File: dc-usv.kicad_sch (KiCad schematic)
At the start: 0 parts

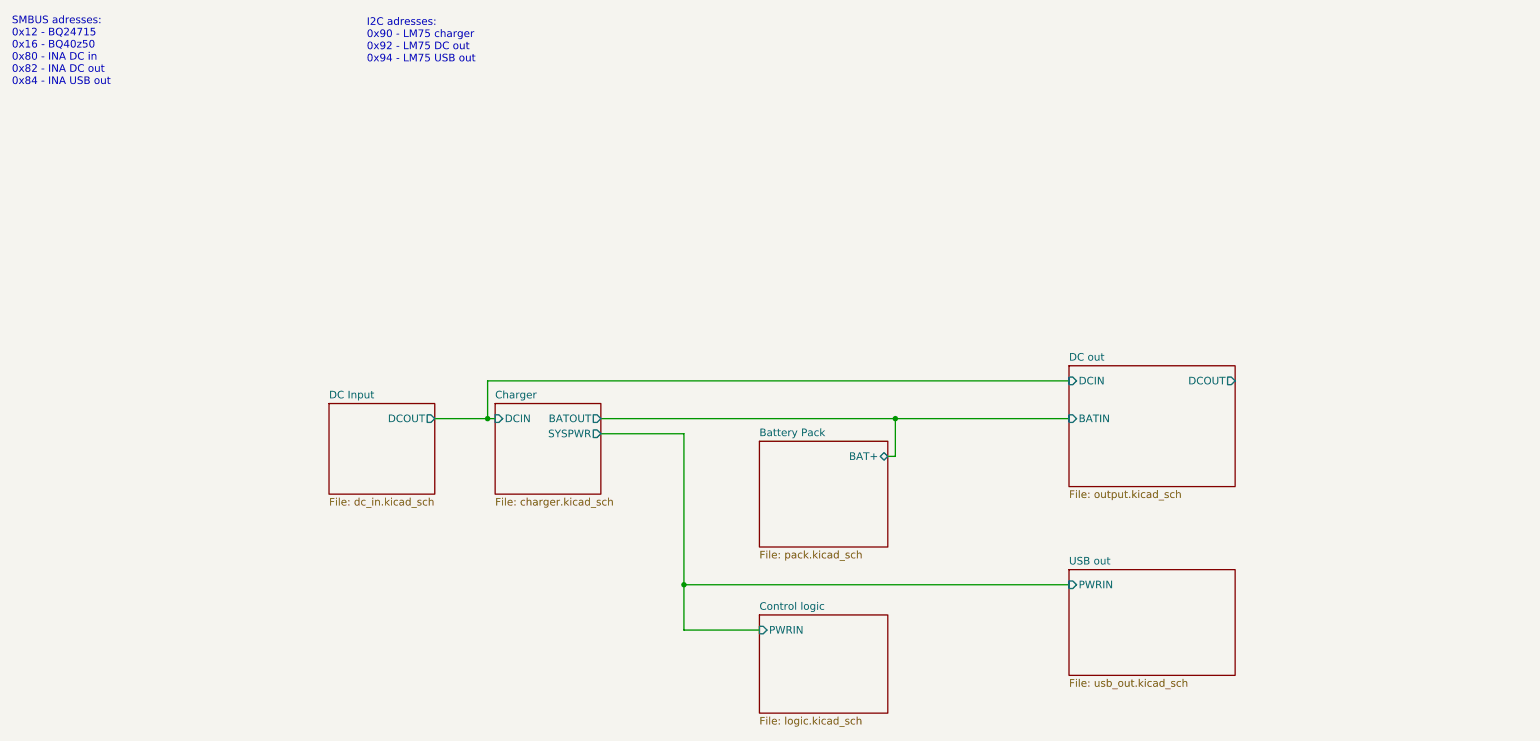
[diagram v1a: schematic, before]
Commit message: Finish DC output schematic capture
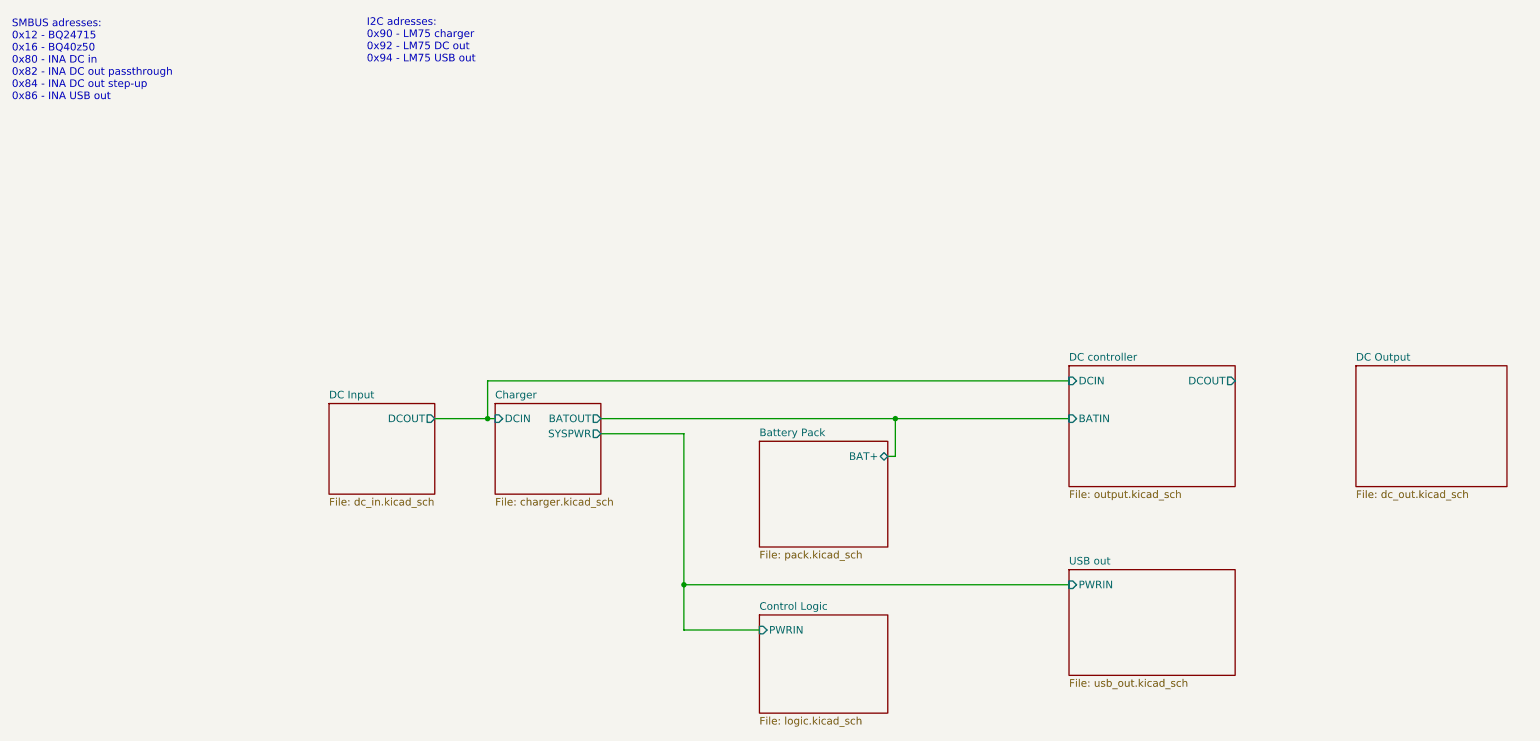
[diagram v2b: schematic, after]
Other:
- sheet Control logic renamed Control Logic
- sheet DC out renamed DC controller
- added sheet DC Output (dc_out.kicad_sch)
- note added: "SMBUS adresses: 0x12 - BQ24715 0x16 - BQ40z50 0x80 - INA DC in 0x82 - INA DC out passthrough 0x84 - INA DC out step-up 0x86 - INA USB out"
- note removed: "SMBUS adresses: 0x12 - BQ24715 0x16 - BQ40z50 0x80 - INA DC in 0x82 - INA DC out 0x84 - INA USB out"

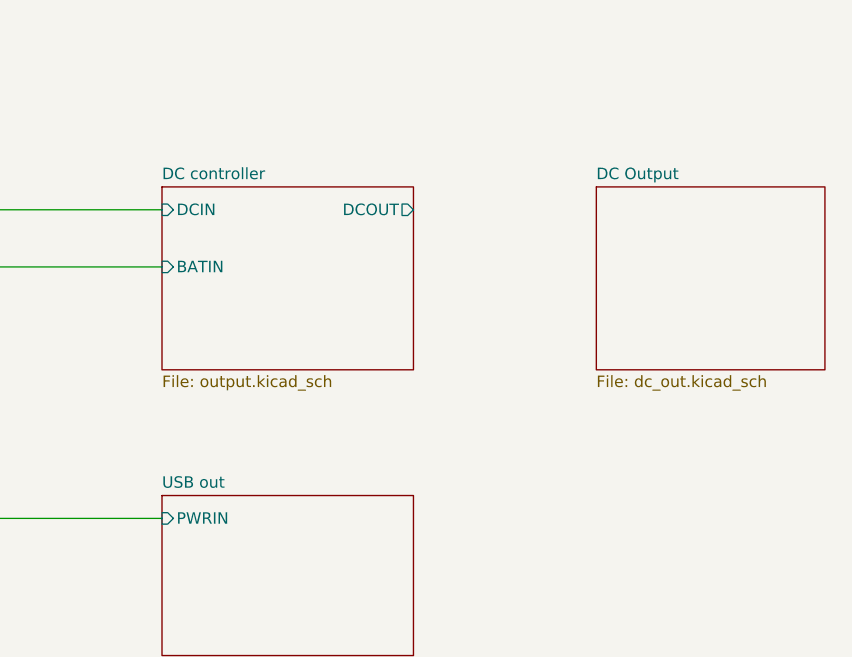
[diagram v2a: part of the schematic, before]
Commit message: Add barrel jack footprints
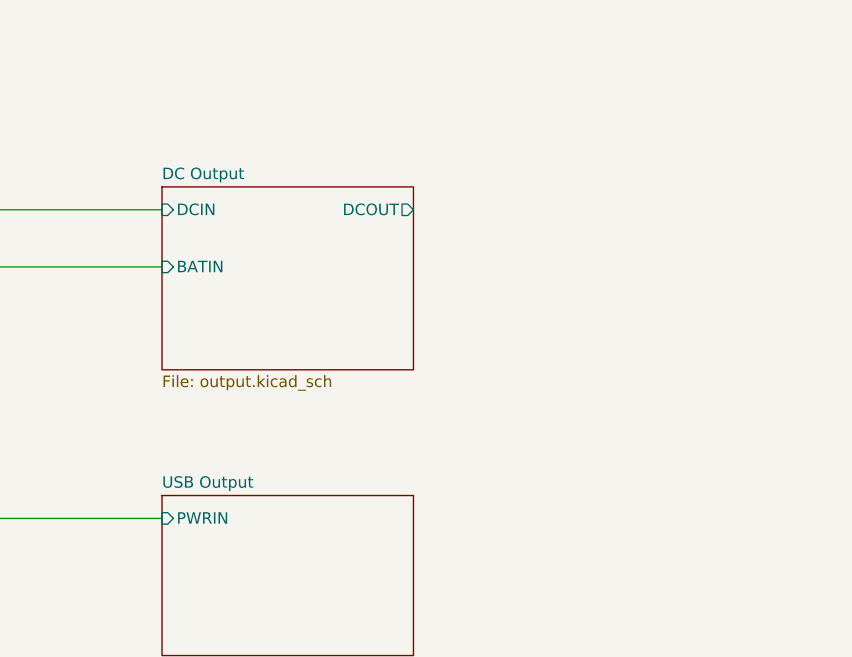
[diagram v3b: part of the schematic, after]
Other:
- sheet USB out renamed USB Output
- removed sheet DC controller
- sheet DC Output: file dc_out.kicad_sch -> output.kicad_sch
- sheet DC Output ports: added BATIN, DCIN, DCOUT; removed none

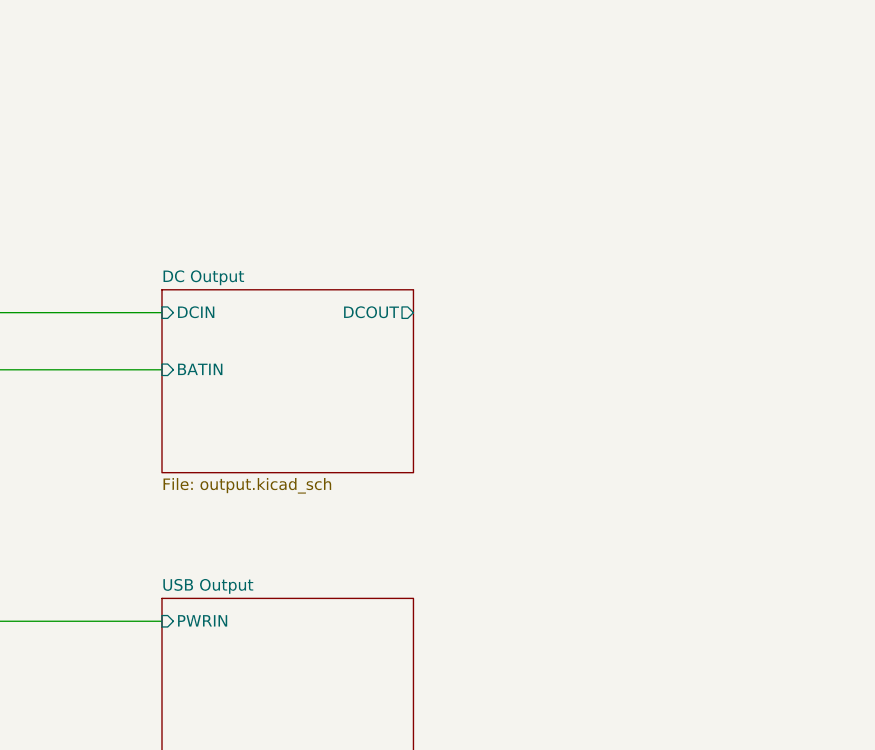
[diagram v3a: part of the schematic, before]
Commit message: Add individually switchable outputs
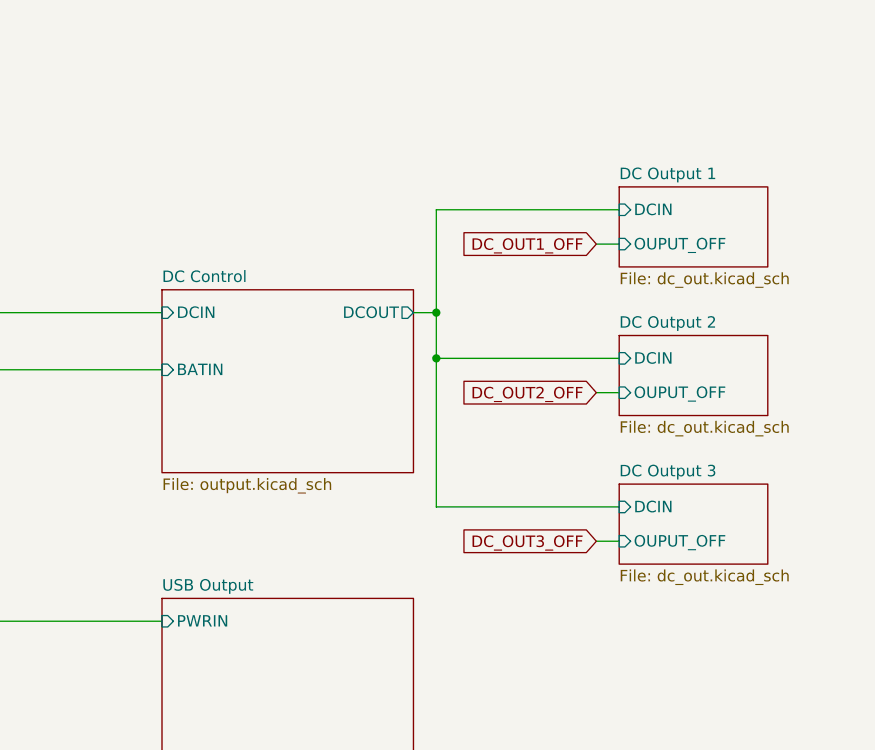
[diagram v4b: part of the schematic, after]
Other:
- sheet DC Output renamed DC Control
- added sheet DC Output 1 (dc_out.kicad_sch)
- added sheet DC Output 2 (dc_out.kicad_sch)
- added sheet DC Output 3 (dc_out.kicad_sch)

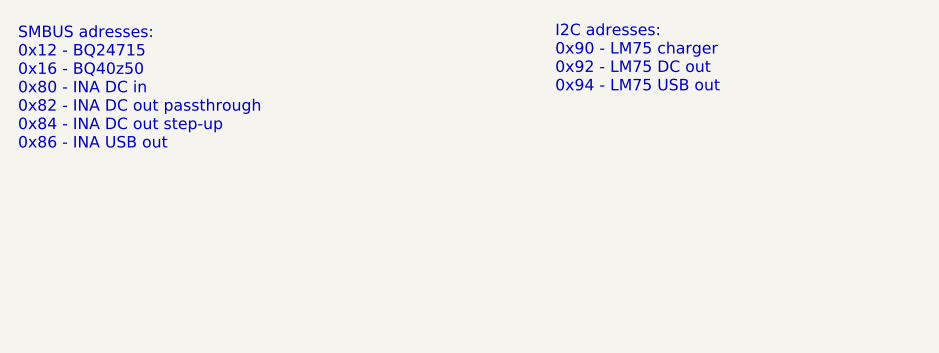
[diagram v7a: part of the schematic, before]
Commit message: Add 64x48 SSD1306 OLED
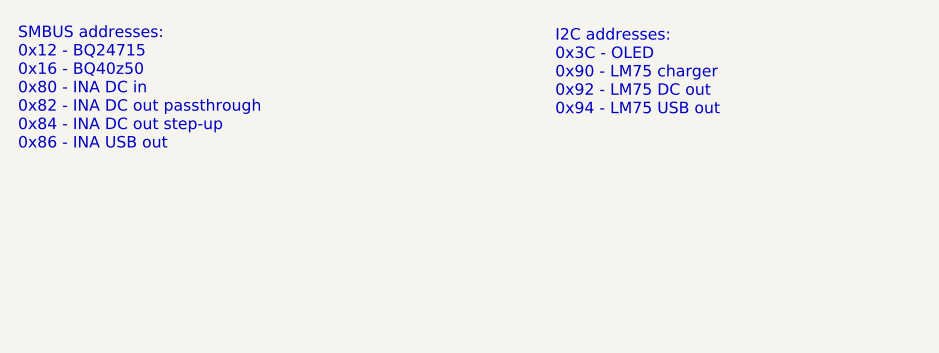
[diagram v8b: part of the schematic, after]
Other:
- note added: "I2C addresses: 0x3C - OLED 0x90 - LM75 charger 0x92 - LM75 DC out 0x94 - LM75 USB out"
- note added: "SMBUS addresses: 0x12 - BQ24715 0x16 - BQ40z50 0x80 - INA DC in 0x82 - INA DC out passthrough 0x84 - INA DC out step-up 0x86 - INA USB out"
- note removed: "I2C adresses: 0x90 - LM75 charger 0x92 - LM75 DC out 0x94 - LM75 USB out"
- note removed: "SMBUS adresses: 0x12 - BQ24715 0x16 - BQ40z50 0x80 - INA DC in 0x82 - INA DC out passthrough 0x84 - INA DC out step-up 0x86 - INA USB out"
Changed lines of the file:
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@@
     (stroke (width 0) (type default) (color 0 0 0 0))
   )
-  (text "I2C adresses:\n0x90 - LM75 charger\n0x92 - LM75 DC out\n0x94 - LM75 USB out"
-    (at 73.66 21.59 0)
+  (text "I2C addresses:\n0x3C - OLED\n0x90 - LM75 charger\n0x92 - LM75 DC out\n0x94 - LM75 USB out"
+    (at 73.66 24.13 0)
     (effects (font (size 1.27 1.27)) (justify left bottom))
   )
-  (text "SMBUS adresses:\n0x12 - BQ24715\n0x16 - BQ40z50\n0x80 - INA DC in\n0x82 - INA DC out passthrough\n0x84 - INA DC out step-up\n0x86 - INA USB out\n"
+  (text "SMBUS addresses:\n0x12 - BQ24715\n0x16 - BQ40z50\n0x80 - INA DC in\n0x82 - INA DC out passthrough\n0x84 - INA DC out step-up\n0x86 - INA USB out\n"
     (at 13.97 27.94 0)
     (effects (font (size 1.27 1.27)) (justify left bottom))
@@
       (reference "#PWR0286") (unit 1) (value "GND1") (footprint "")
     )
+    (path "/a06395f1-7afb-45e9-b1be-eb1d60bae674/864d4d48-6f72-42a3-8bf5-0e9f3bf6ac04"
+      (reference "#PWR0287") (unit 1) (value "GND") (footprint "")
+    )
+    (path "/a06395f1-7afb-45e9-b1be-eb1d60bae674/100a0824-a0bd-41ac-9aca-e268953348c2"
+      (reference "#PWR0288") (unit 1) (value "GND") (footprint "")
+    )
+    (path "/a06395f1-7afb-45e9-b1be-eb1d60bae674/d3c3c1b3-e212-4b13-ab8a-3da11c6ea3ae"
+      (reference "#PWR0289") (unit 1) (value "GND") (footprint "")
+    )
+    (path "/a06395f1-7afb-45e9-b1be-eb1d60bae674/3fd45b3e-2789-4f87-a714-a38bf8c3c082"
+      (reference "#PWR0290") (unit 1) (value "GND") (footprint "")
+    )
+    (path "/a06395f1-7afb-45e9-b1be-eb1d60bae674/c3bc4531-d7eb-4659-bcc5-4495596eec0e"
+      (reference "#PWR0291") (unit 1) (value "GND") (footprint "")
+    )
+    (path "/a06395f1-7afb-45e9-b1be-eb1d60bae674/96c21d38-2693-49eb-8c0f-b5b5e9b32aac"
+      (reference "#PWR0292") (unit 1) (value "+3V3") (footprint "")
+    )
+    (path "/a06395f1-7afb-45e9-b1be-eb1d60bae674/5c378547-1d50-4027-9acb-9cc03482ba48"
+      (reference "#PWR0293") (unit 1) (value "+3V3") (footprint "")
+    )
+    (path "/a06395f1-7afb-45e9-b1be-eb1d60bae674/0eab53e8-affc-4690-9107-cc5833df24df"
+      (reference "#PWR0294") (unit 1) (value "GND") (footprint "")
+    )
+    (path "/a06395f1-7afb-45e9-b1be-eb1d60bae674/b3b4c5c1-ec24-4743-af6c-eb2bd65f44f7"
+      (reference "#PWR0295") (unit 1) (value "GND") (footprint "")
+    )
+    (path "/a06395f1-7afb-45e9-b1be-eb1d60bae674/5b7aaa49-43f6-4ce3-b718-b535fac26f74"
+      (reference "#PWR0296") (unit 1) (value "+3V3") (footprint "")
+    )
     (path "/aa145c2f-e167-4de3-92bf-3e0d0ae2fb67/06ec14b7-6af4-46b3-aed4-1258a100ed19"
       (reference "B1") (unit 1) (value "18650") (footprint "battery-holder-keystone:SMD-1048-dual-18650")
@@
       (reference "C95") (unit 1) (value "22nF") (footprint "Capacitor_SMD:C_0402_1005Metric")
     )
+    (path "/a06395f1-7afb-45e9-b1be-eb1d60bae674/65dad363-8230-4815-8554-9e232279028e"
+      (reference "C96") (unit 1) (value "100nF") (footprint "Capacitor_SMD:C_0402_1005Metric")
+    )
+    (path "/a06395f1-7afb-45e9-b1be-eb1d60bae674/5c96e53a-5201-40ec-abac-977e940adb95"
+      (reference "C97") (unit 1) (value "1uF") (footprint "Capacitor_SMD:C_0402_1005Metric")
+    )
+    (path "/a06395f1-7afb-45e9-b1be-eb1d60bae674/fb029d2f-ce1a-4293-9239-39f8f07605b4"
+      (reference "C98") (unit 1) (value "1uF") (footprint "Capacitor_SMD:C_0402_1005Metric")
+    )
+    (path "/a06395f1-7afb-45e9-b1be-eb1d60bae674/dc7e8264-626f-4f27-9cd6-b5f69c3cb504"
+      (reference "C99") (unit 1) (value "100nF") (footprint "Capacitor_SMD:C_0402_1005Metric")
+    )
+    (path "/a06395f1-7afb-45e9-b1be-eb1d60bae674/daf0f95a-b181-49b3-86b6-6f49300762eb"
+      (reference "C100") (unit 1) (value "10uF LV") (footprint "Capacitor_SMD:C_0402_1005Metric")
+    )
+    (path "/a06395f1-7afb-45e9-b1be-eb1d60bae674/80de1fff-82f5-43cb-87c7-c3789c73511a"
+      (reference "C101") (unit 1) (value "100nF") (footprint "Capacitor_SMD:C_0402_1005Metric")
+    )
+    (path "/a06395f1-7afb-45e9-b1be-eb1d60bae674/0f92f848-e9cc-41fe-bcd6-3093c3779c6a"
+      (reference "C102") (unit 1) (value "4.7uF HV") (footprint "Capacitor_SMD:C_0603_1608Metric")
+    )
+    (path "/a06395f1-7afb-45e9-b1be-eb1d60bae674/3306a8e7-9ac6-4828-a859-595b3c1e292a"
+      (reference "C103") (unit 1) (value "2.2uF") (footprint "Capacitor_SMD:C_0603_1608Metric")
+    )
     (path "/aa145c2f-e167-4de3-92bf-3e0d0ae2fb67/defc8839-bf1e-4b04-89fc-3cffafd43258"
       (reference "D1") (unit 1) (value "1N4148WS") (footprint "Diode_SMD:D_SOD-323")
@@
       (reference "R115") (unit 1) (value "10k") (footprint "Resistor_SMD:R_0402_1005Metric")
     )
+    (path "/a06395f1-7afb-45e9-b1be-eb1d60bae674/29c11fbb-2da6-4e6d-ae77-07acceba4911"
+      (reference "R116") (unit 1) (value "100kR") (footprint "Resistor_SMD:R_0402_1005Metric")
+    )
+    (path "/a06395f1-7afb-45e9-b1be-eb1d60bae674/334c4c1c-aafa-445a-8268-9f20ace4b652"
+      (reference "R117") (unit 1) (value "390kR") (footprint "Resistor_SMD:R_0603_1608Metric")
+    )
     (path "/4ce9e4d8-553f-40e6-a397-66d04db306f8/3152910b-dfc7-4fc7-87ab-336be9ca10d0"
       (reference "SW1") (unit 1) (value "SW_DIP_x02") (footprint "Connector_PinHeader_2.54mm:PinHeader_2x02_P2.54mm_Vertical")
@@
       (reference "U16") (unit 1) (value "CH340G") (footprint "Package_SO:SOIC-16_3.9x9.9mm_P1.27mm")
     )
+    (path "/a06395f1-7afb-45e9-b1be-eb1d60bae674/09d6e4a2-a135-4aa7-a5c0-b78a7e1387c0"
+      (reference "U17") (unit 1) (value "N066-6448TSWEG03-H28") (footprint "Display_OLED:N066-6448TSWEG03-H28")
+    )
     (path "/a06395f1-7afb-45e9-b1be-eb1d60bae674/b2d83311-3769-443b-9605-bbef8899a620/c8035e2e-1a39-416d-bfe6-a3df66d2a4a2"
